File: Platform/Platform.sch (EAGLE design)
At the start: 30 parts, among them U1 LCD-16X2SILK, U2 LM2574N, X1 USBSMD, Y1 RESONATORSMD

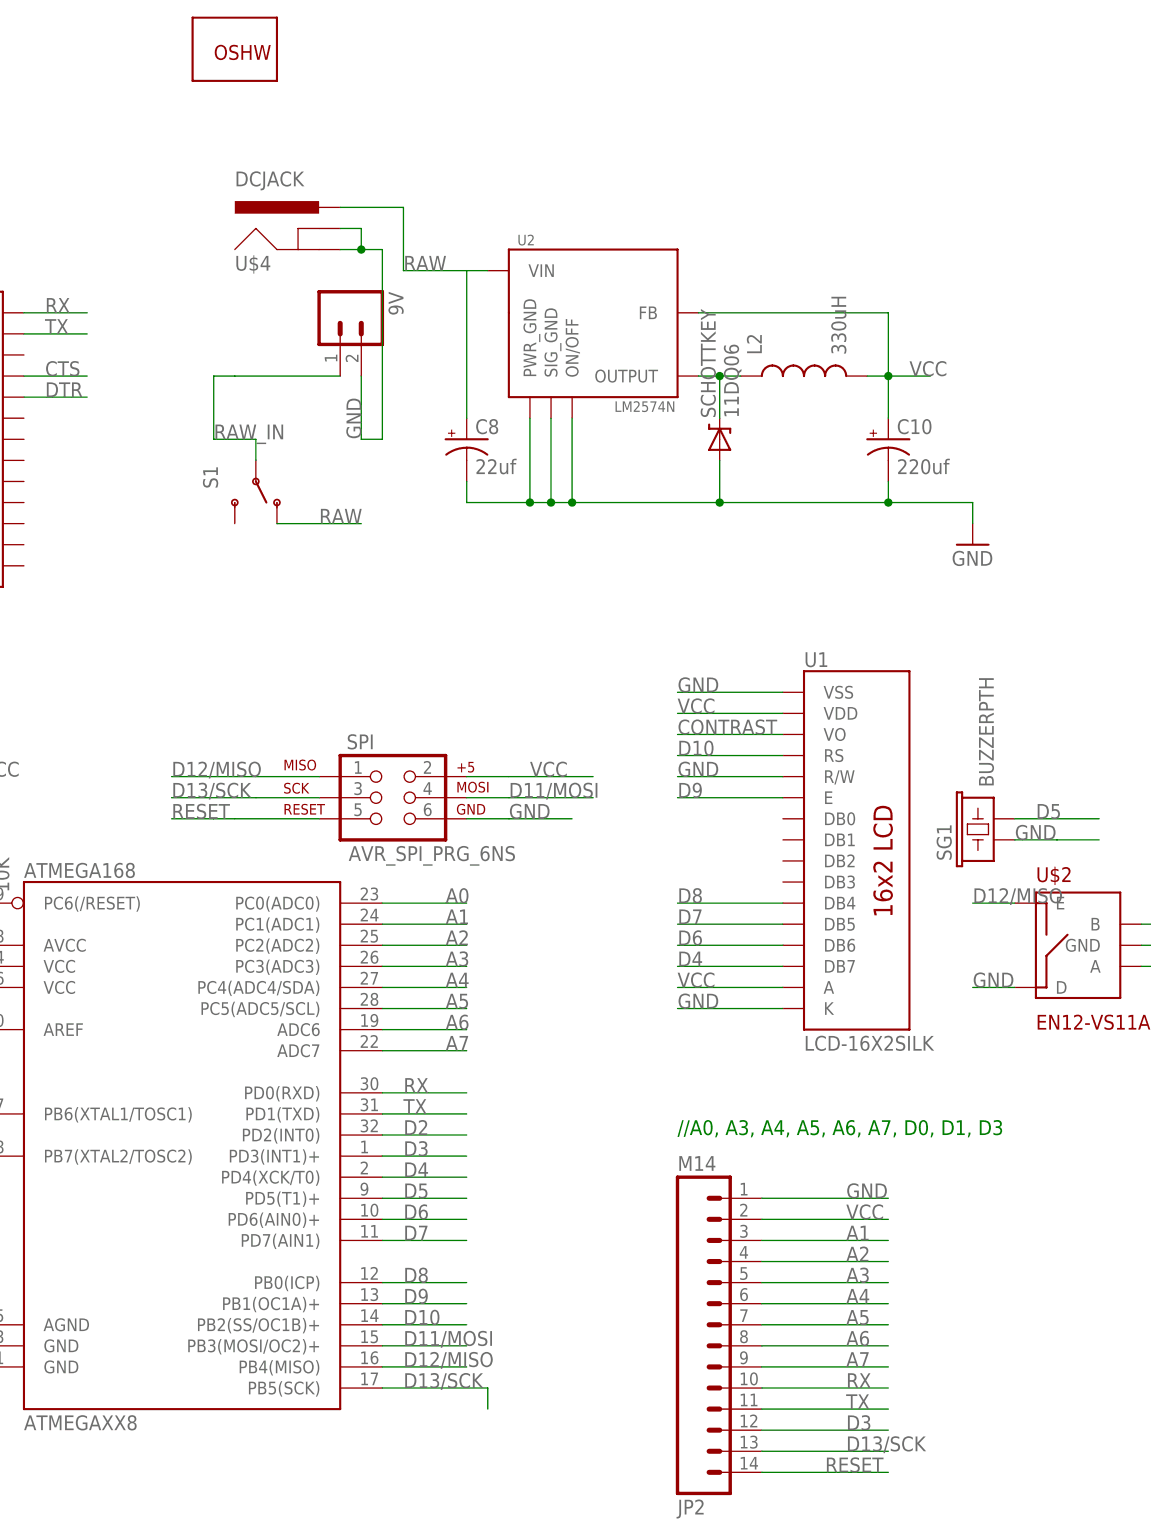
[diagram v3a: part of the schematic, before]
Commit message: More board tweak, added part list and toner file used to make pre prototype 2
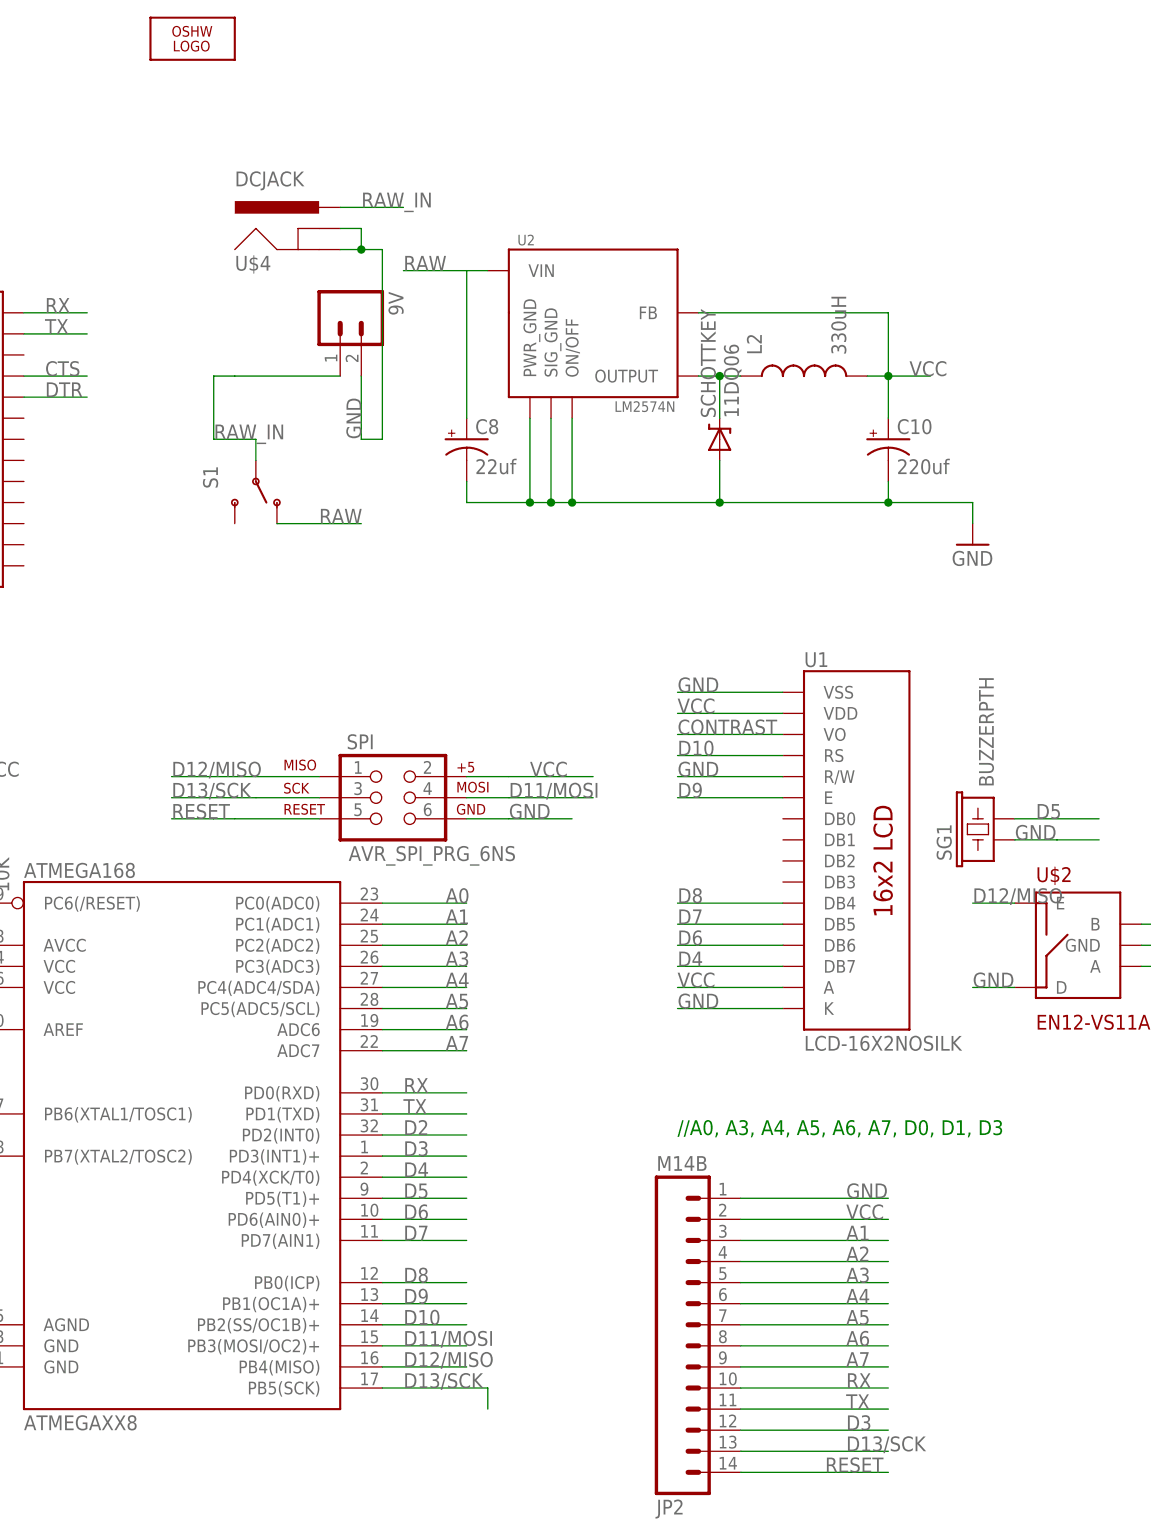
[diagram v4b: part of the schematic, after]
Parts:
- removed GOLD_ORB_SM1: OSHWLOGO_GOLD_ORB_SM, NBitWonder:OSHWLOGO_GOLD_ORB_SM
- added LOGO1: OSHW_LOGO_10MIL, ohw-logo:OSHW_LOGO_10MIL
- JP2: value M14 -> M14B; device SparkFun:M14 -> Dustin:M14B
- U1: value LCD-16X2SILK -> LCD-16X2NOSILK; device SparkFun:LCD-16X2SILK -> SparkFun:LCD-16X2NOSILK
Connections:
- net RAW: no longer U$4.PWR
- net RAW_IN: now also U$4.PWR
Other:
- moved on the sheet: JP2

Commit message: prototype 3
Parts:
- removed C10: 220uf, SparkFun:CAP_POLPTH1
- removed C7: 4.7uf, SparkFun:CAP_POLPTH1
- removed LOGO1: OSHW_LOGO_10MIL, ohw-logo:OSHW_LOGO_10MIL
- removed SG1: BUZZERPTH, SparkFun:BUZZERPTH
- removed U1: LCD-16X2NOSILK, SparkFun:LCD-16X2NOSILK
- added C4: 68uf, Dustin:CAP_POLF80
- added C5: 120uf, Dustin:CAP_POL8X10
- added JP1: M14B, Dustin:M14B
- added LCDCON: (no value), con-harting:CON14
- added LED2: RED, SparkFun:LED1206
- added LINK1, LINK2, LINK3, LINK4: LINK, Dustin:LINK
- added R4: TRIMPOTSMD, SparkFun:TRIMPOTSMD
- added SG2: BUZZERSMD, SparkFun:BUZZERSMD
- C8: value 22uf -> 4.7uf; device SparkFun:CAP_POLPTH1 -> Dustin:CAP_POLCAP-B
- L2: value 330uH -> 100uH; device SparkFun:INDUCTOR1206H* -> SparkFun:INDUCTOR0805
- LED1: value (none) -> GRN; device SparkFun:LED3MM -> SparkFun:LED1206
- R3: value 10k -> 220; device SparkFun:TRIMPOTPTH -> SparkFun:RESISTOR0805-RES
- SCHOTTKEY: value 11DQ06 -> DIODE-SCHOTTKY; device SparkFun:DIODE-ZENERPTH -> Dustin:DIODE-SCHOTTKY
- U$1: value FT232RL -> FT232RLSSOP; device Dustin:FT232RL -> Dustin:FT232RLSSOP
- U$4: value DCJACK -> DCJACKSMD; device Dustin:DCJACK -> Dustin:DCJACKSMD
- U2: device Dustin:LM2574N -> Dustin:LM2574NSOIC8
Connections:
- removed net CTS: U$1.CTS#
- new net FTDI-GND: C8.-, C9.1, LINK4.P$2, U$1.AGND, U$1.CTS#, U$1.GND, U$1.TEST
- new net FTDI-VCC: C6.-, C8.+, LINK3.P$1, U$1.VCC, U$1.VCCIO, U$3.P$2, X1.GND
- new net GNDLINK: C4.-, C5.-, LINK2.P$1, SCHOTTKEY.A, U2.ON/OFF, U2.PWR_GND, U2.SIG_GND
- new net N$7: LED1.C, R3.2
- new net VCCLINK: C5.+, L2.2, LINK1.P$1, U2.FB
- net A1: now also JP1.3
- net A2: now also JP1.4
- net A3: now also JP1.5
- net A4: now also JP1.6
- net A5: now also JP1.7
- net A6: now also JP1.8
- net A7: now also JP1.9
- net CONTRAST: now also LCDCON.3, R4.WIPER; no longer R3.WIPER, U1.VO
- net D10: now also LCDCON.4; no longer U1.RS
- net D13/SCK: now also JP1.13, LED2.A; no longer LED1.A
- net D3: now also JP1.12
- net D4: now also LCDCON.14; no longer U1.DB7
- net D5: now also SG2.2; no longer SG1.2
- net D6: now also LCDCON.13; no longer U1.DB6
- net D7: now also LCDCON.12; no longer U1.DB5
- net D8: now also LCDCON.11; no longer U1.DB4
- net D9: now also LCDCON.6; no longer U1.E
- net GND: now also JP1.1, LCDCON.1, LCDCON.5, LINK2.P$2, LINK4.P$1, R3.1, R4.CW, SG2.1; no longer C10.-, C6.-, C7.-, C8.-, C9.1, R3.CW, SCHOTTKEY.A, SG1.1, U$1.AGND, U$1.GND, U$1.TEST, U1.K, U1.R/W, U1.VSS, U2.ON/OFF, U2.PWR_GND, U2.SIG_GND, X1.GND
- net N$2: now also LED2.C; no longer LED1.C
- net RAW: now also C4.+; no longer C8.+
- net RESET: now also JP1.14
- net RX: now also JP1.10
- net TX: now also JP1.11
- net VCC: now also JP1.2, LCDCON.2, LED1.A, LINK1.P$2, LINK3.P$2, R4.CCW; no longer C10.+, C7.+, L2.2, R3.CCW, U$1.VCC, U$1.VCCIO, U$3.P$2, U1.A, U1.VDD, U2.FB
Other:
- moved on the sheet: LED1

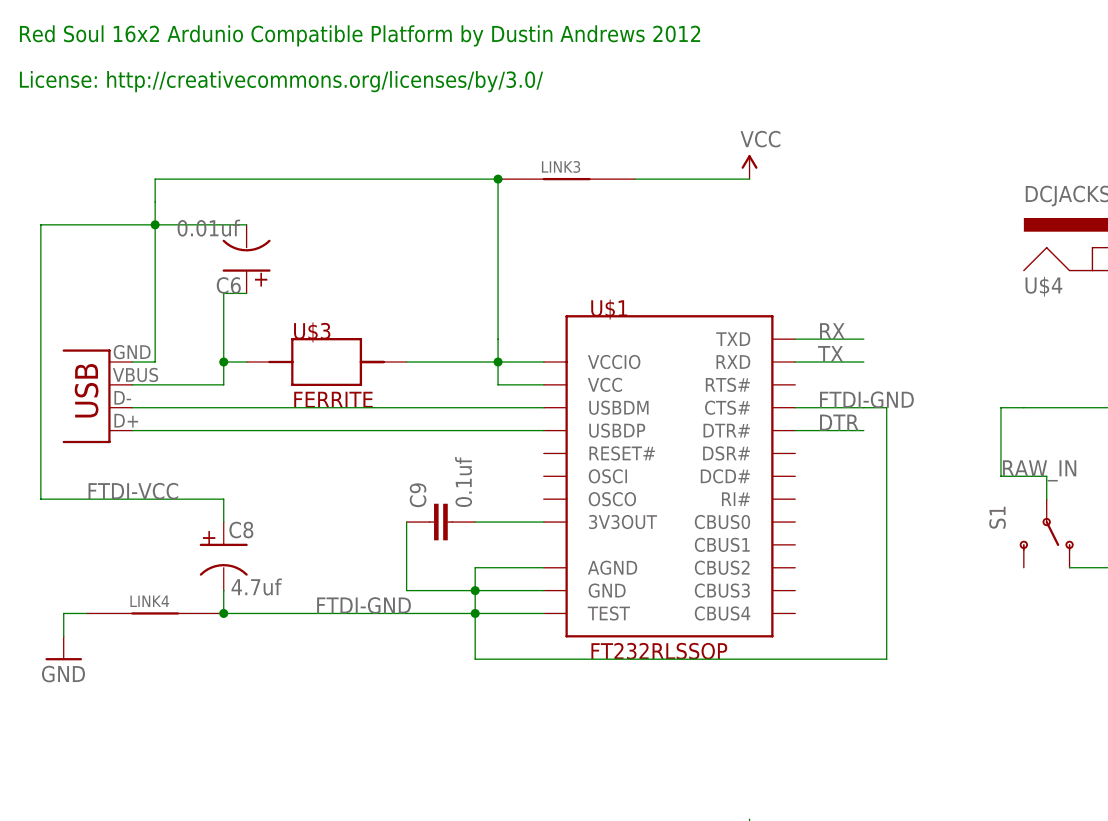
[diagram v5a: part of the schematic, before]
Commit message: Fixed some issues with the FTDI. Created Gerbers. Sent version off for manufacture.
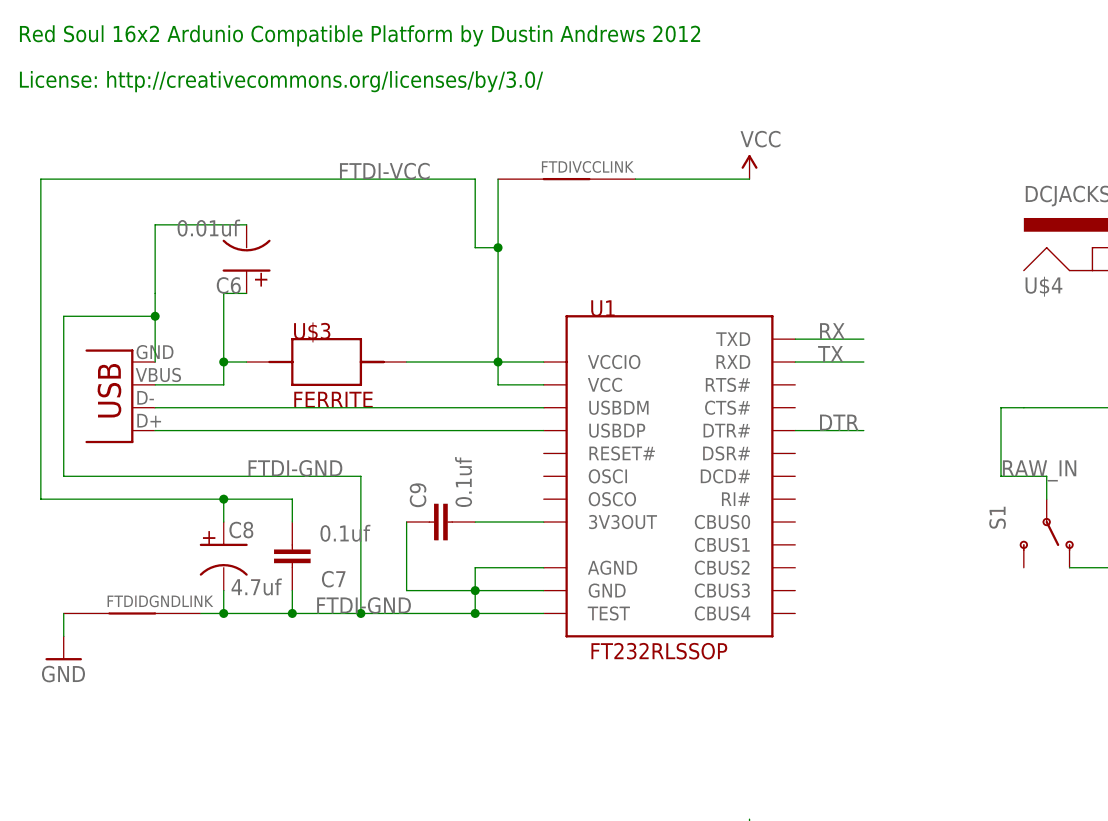
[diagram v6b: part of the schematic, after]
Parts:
- removed LINK4: LINK, Dustin:LINK
- added C7: 0.1uf, SparkFun:CAP0805
- added FTDIDGNDLINK: LINK, Dustin:LINK
- renumbered LINK3 to FTDIVCCLINK, U$1 to U1
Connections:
- net N$1 renamed VBUS
- net N$4 renamed D-
- net N$5 renamed D+
- net N$6 renamed 3V3OUT
- net FTDI-GND: now also C6.-, C7.1, FTDIDGNDLINK.P$2, X1.GND; no longer LINK4.P$2, U1.CTS#
- net FTDI-VCC: now also C7.2; no longer C6.-, X1.GND
- net GND: now also FTDIDGNDLINK.P$1; no longer LINK4.P$1
